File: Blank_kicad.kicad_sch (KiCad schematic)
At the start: 4 parts

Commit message: Anotate a symbol
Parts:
- R1: renamed from R?; value (none) -> R
- gave numbers to parts that had none: 3
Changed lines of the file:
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@@
   (symbol (lib_id "Device:R") (at 87.63 99.06 0) (unit 1)
     (in_bom yes) (on_board yes) (fields_autoplaced)
-    (property "Reference" "R?" (id 0) (at 90.17 97.7899 0)
+    (property "Reference" "R1" (id 0) (at 90.17 97.7899 0)
       (effects (font (size 1.27 1.27)) (justify left))
     )
-    (property "Value" "" (id 1) (at 90.17 100.3299 0)
+    (property "Value" "R" (id 1) (at 90.17 100.3299 0)
       (effects (font (size 1.27 1.27)) (justify left))
     )
@@
   (symbol (lib_id "Device:R") (at 128.27 99.06 0) (unit 1)
     (in_bom yes) (on_board yes) (fields_autoplaced)
-    (property "Reference" "R?" (id 0) (at 130.81 97.7899 0)
+    (property "Reference" "R3" (id 0) (at 130.81 97.7899 0)
       (effects (font (size 1.27 1.27)) (justify left))
     )
@@
   (symbol (lib_id "Device:R") (at 105.41 100.33 0) (unit 1)
     (in_bom yes) (on_board yes) (fields_autoplaced)
-    (property "Reference" "R?" (id 0) (at 107.95 99.0599 0)
+    (property "Reference" "R2" (id 0) (at 107.95 99.0599 0)
       (effects (font (size 1.27 1.27)) (justify left))
     )
@@
   (symbol (lib_id "Device:R") (at 144.78 100.33 0) (unit 1)
     (in_bom yes) (on_board yes) (fields_autoplaced)
-    (property "Reference" "R?" (id 0) (at 147.32 99.0599 0)
+    (property "Reference" "R4" (id 0) (at 147.32 99.0599 0)
       (effects (font (size 1.27 1.27)) (justify left))
     )
@@
   (symbol_instances
     (path "/065b9982-55f2-4822-977e-07e8a06e7b35"
-      (reference "R?") (unit 1) (value "R") (footprint "")
+      (reference "R1") (unit 1) (value "R") (footprint "")
+    )
+    (path "/0f62e92c-dce6-45dc-a560-b9db10f66ff3"
+      (reference "R2") (unit 1) (value "R") (footprint "")
     )
     (path "/086ab04d-4086-427c-992f-819b91a9021d"
-      (reference "R?") (unit 1) (value "R") (footprint "")
-    )
-    (path "/0f62e92c-dce6-45dc-a560-b9db10f66ff3"
-      (reference "R?") (unit 1) (value "R") (footprint "")
+      (reference "R3") (unit 1) (value "R") (footprint "")
     )
     (path "/5841a60a-7434-4694-9b2f-60c2321b8bd0"
-      (reference "R?") (unit 1) (value "R") (footprint "")
+      (reference "R4") (unit 1) (value "R") (footprint "")
     )
   )

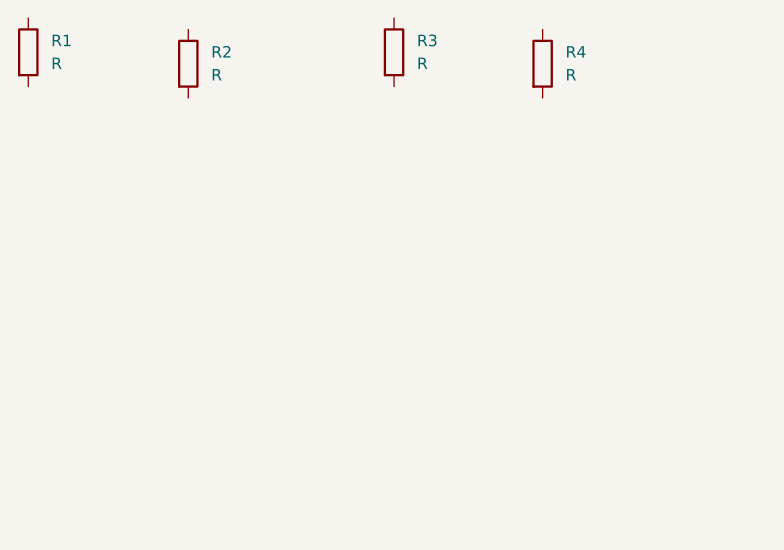
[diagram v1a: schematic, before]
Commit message: Anotate a  capacitor symbol
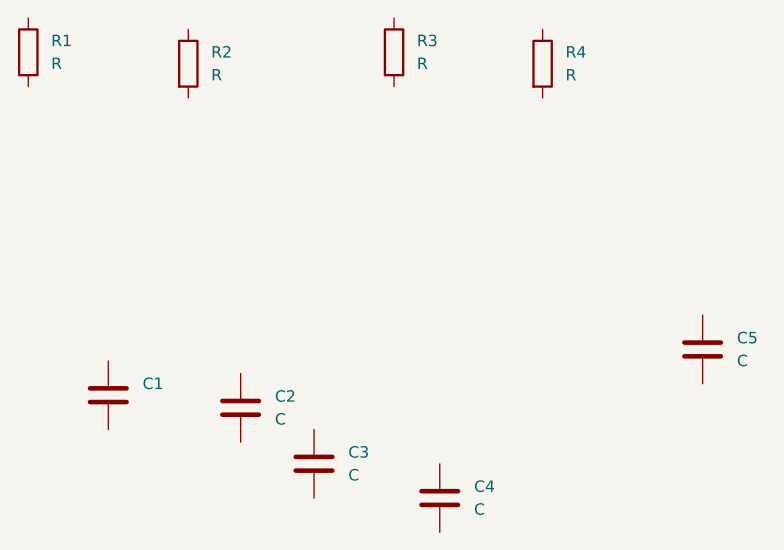
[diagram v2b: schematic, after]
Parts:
- added C1: (no value), symbol Device:C
- added C2, C3, C4, C5: C, symbol Device:C
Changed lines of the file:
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@@
+    (pin "2")
+  )
+  (symbol (lib_id "Device:C") (at 96.52 137.16 0) (unit 1)
+    (in_bom yes) (on_board yes) (fields_autoplaced)
+    (property "Reference" "C1" (id 0) (at 100.33 135.8899 0)
+      (effects (font (size 1.27 1.27)) (justify left))
+    )
+    (property "Value" "" (id 1) (at 100.33 138.4299 0)
+      (effects (font (size 1.27 1.27)) (justify left))
+    )
+    (property "Footprint" "" (id 2) (at 97.4852 140.97 0)
+      (effects (font (size 1.27 1.27)) hide)
+    )
+    (property "Datasheet" "~" (id 3) (at 96.52 137.16 0)
+      (effects (font (size 1.27 1.27)) hide)
+    )
+    (pin "1")
+    (pin "2")
+  )
+  (symbol (lib_id "Device:C") (at 119.38 144.78 0) (unit 1)
+    (in_bom yes) (on_board yes) (fields_autoplaced)
+    (property "Reference" "C3" (id 0) (at 123.19 143.5099 0)
+      (effects (font (size 1.27 1.27)) (justify left))
+    )
+    (property "Value" "C" (id 1) (at 123.19 146.0499 0)
+      (effects (font (size 1.27 1.27)) (justify left))
+    )
+    (property "Footprint" "" (id 2) (at 120.3452 148.59 0)
+      (effects (font (size 1.27 1.27)) hide)
+    )
+    (property "Datasheet" "~" (id 3) (at 119.38 144.78 0)
+      (effects (font (size 1.27 1.27)) hide)
+    )
+    (pin "1")
     (pin "2")
   )
@@
     (pin "2")
   )
+  (symbol (lib_id "Device:C") (at 111.2251 138.5674 0) (unit 1)
+    (in_bom yes) (on_board yes) (fields_autoplaced)
+    (property "Reference" "C2" (id 0) (at 115.0351 137.2973 0)
+      (effects (font (size 1.27 1.27)) (justify left))
+    )
+    (property "Value" "C" (id 1) (at 115.0351 139.8373 0)
+      (effects (font (size 1.27 1.27)) (justify left))
+    )
+    (property "Footprint" "" (id 2) (at 112.1903 142.3774 0)
+      (effects (font (size 1.27 1.27)) hide)
+    )
+    (property "Datasheet" "~" (id 3) (at 111.2251 138.5674 0)
+      (effects (font (size 1.27 1.27)) hide)
+    )
+    (pin "1")
+    (pin "2")
+  )
+  (symbol (lib_id "Device:C") (at 162.56 132.08 0) (unit 1)
+    (in_bom yes) (on_board yes) (fields_autoplaced)
+    (property "Reference" "C5" (id 0) (at 166.37 130.8099 0)
+      (effects (font (size 1.27 1.27)) (justify left))
+    )
+    (property "Value" "C" (id 1) (at 166.37 133.3499 0)
+      (effects (font (size 1.27 1.27)) (justify left))
+    )
+    (property "Footprint" "" (id 2) (at 163.5252 135.89 0)
+      (effects (font (size 1.27 1.27)) hide)
+    )
+    (property "Datasheet" "~" (id 3) (at 162.56 132.08 0)
+      (effects (font (size 1.27 1.27)) hide)
+    )
+    (pin "1")
+    (pin "2")
+  )
+  (symbol (lib_id "Device:C") (at 133.35 148.59 0) (unit 1)
+    (in_bom yes) (on_board yes) (fields_autoplaced)
+    (property "Reference" "C4" (id 0) (at 137.16 147.3199 0)
+      (effects (font (size 1.27 1.27)) (justify left))
+    )
+    (property "Value" "C" (id 1) (at 137.16 149.8599 0)
+      (effects (font (size 1.27 1.27)) (justify left))
+    )
+    (property "Footprint" "" (id 2) (at 134.3152 152.4 0)
+      (effects (font (size 1.27 1.27)) hide)
+    )
+    (property "Datasheet" "~" (id 3) (at 133.35 148.59 0)
+      (effects (font (size 1.27 1.27)) hide)
+    )
+    (pin "1")
+    (pin "2")
+  )
   (sheet_instances
     (path "/" (page "1"))
   )
   (symbol_instances
+    (path "/2231b7ac-f92b-4941-9374-f0bfb259582f"
+      (reference "C1") (unit 1) (value "C") (footprint "")
+    )
+    (path "/80dd68ce-19f1-43e0-b3ab-1ab0c515cbd3"
+      (reference "C2") (unit 1) (value "C") (footprint "")
+    )
+    (path "/4f6c8b78-eb1c-4f0a-8689-6fa04cad4d25"
+      (reference "C3") (unit 1) (value "C") (footprint "")
+    )
+    (path "/9cb35d60-e2a6-4cef-b26f-35c25d9959a4"
+      (reference "C4") (unit 1) (value "C") (footprint "")
+    )
+    (path "/9a9d0f27-659c-4a5d-89da-a015ce1d23c4"
+      (reference "C5") (unit 1) (value "C") (footprint "")
+    )
     (path "/065b9982-55f2-4822-977e-07e8a06e7b35"
       (reference "R1") (unit 1) (value "R") (footprint "")
